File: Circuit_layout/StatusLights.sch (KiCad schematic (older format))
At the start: 6 parts

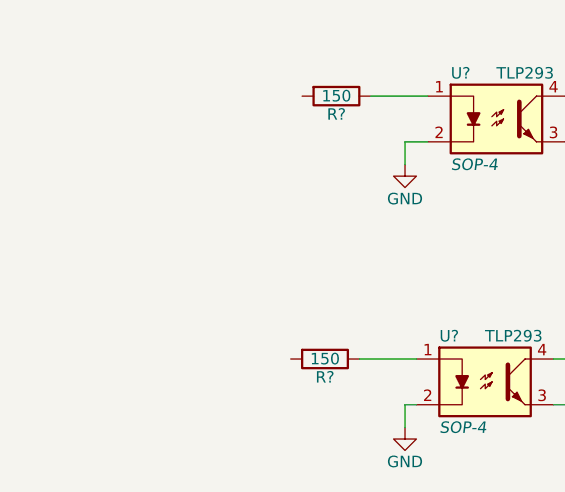
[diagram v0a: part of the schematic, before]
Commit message: adding pinouts to uController
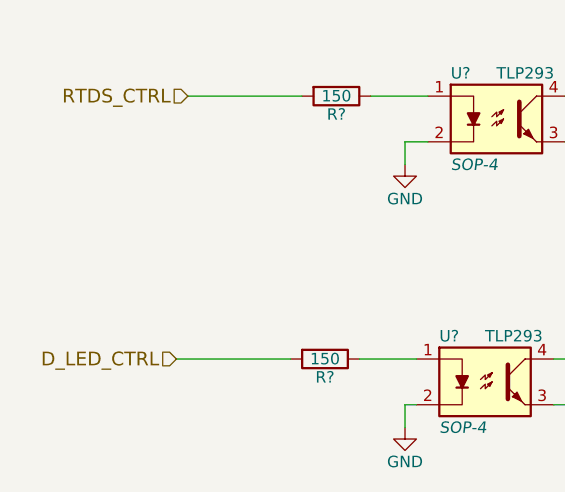
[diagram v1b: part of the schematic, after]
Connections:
- net RTDS_CTRL: now reaches R?.2
- net D_LED_CTRL: now reaches R?.2
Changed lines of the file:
@@
 Wire Wire Line
 	6450 1850 6450 1700
+Wire Wire Line
+	4600 1850 4100 1850
+Wire Wire Line
+	4550 3000 4050 3000
+Text HLabel 4050 3000 0    60   Input ~ 0
+D_LED_CTRL
+Text HLabel 4100 1850 0    60   Input ~ 0
+RTDS_CTRL
 $EndSCHEMATC

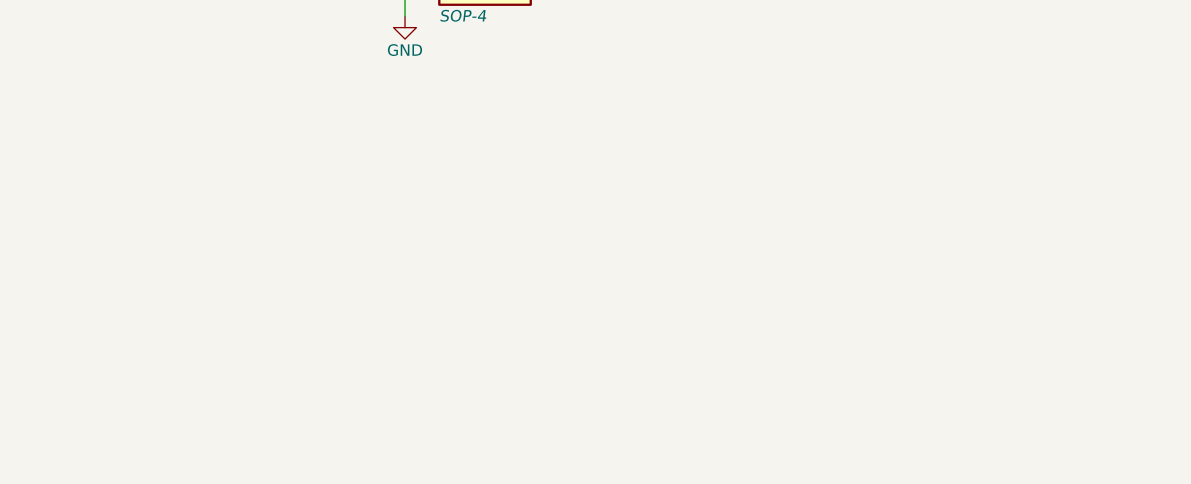
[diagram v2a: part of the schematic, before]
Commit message: added iso circuits, curr. sensor diff amp, IMD fault lt circuit, updated labels
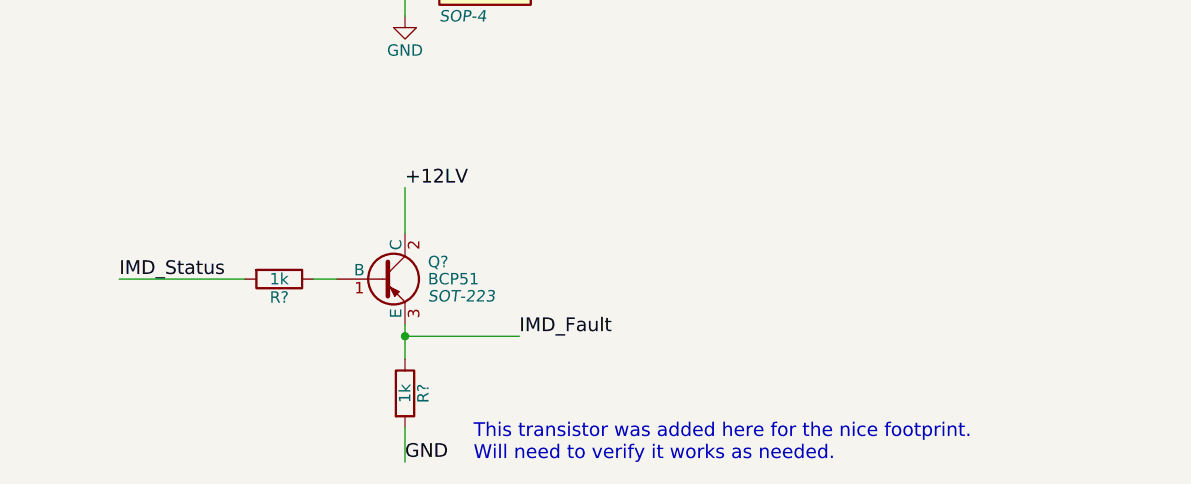
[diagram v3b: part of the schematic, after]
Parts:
- added Q?: BCP51, SOT-223, symbol BCP51
- added R? (x2): 1k, symbol R
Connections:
- net GND: now also R?.2
- new net: Q?.1 (B), R?.1
- new net +12LV: Q?.2 (C)
- new net IMD_Fault: Q?.3 (E), R?.1
- new net IMD_Status: R?.2
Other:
- note added: "This transistor was added here for the nice footprint.\nWill need to verify it works as needed."
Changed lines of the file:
@@
 EESchema Schematic File Version 2
 LIBS:Circuit_layout-rescue
+LIBS:TSI_KiCad_Lib
 LIBS:TSI_HV_Isolater-cache
 LIBS:74xgxx
@@
 $Descr A4 11693 8268
 encoding utf-8
-Sheet 5 7
+Sheet 4 7
 Title "Tractive System Interface"
 Date ""
@@
 Text HLabel 4100 1850 0    60   Input ~ 0
 RTDS_CTRL
+$Comp
+L BCP51 Q?
+U 1 1 58B1C300
+P 4950 4450
+F 0 "Q?" H 5150 4525 50  0000 L CNN
+F 1 "BCP51" H 5150 4450 50  0000 L CNN
+F 2 "SOT-223" H 5150 4375 50  0000 L CIN
+F 3 "" H 4950 4450 50  0000 L CNN
+	1    4950 4450
+	1    0    0    -1
+$EndComp
+Text Notes 5350 5250 0    60   ~ 0
+This transistor was added here for the nice footprint.\nWill need to verify it works as needed.
+Wire Wire Line
+	5050 4250 5050 4050
+$Comp
+L R R?
+U 1 1 58B1C4A9
+P 5050 4950
+F 0 "R?" V 5130 4950 50  0000 C CNN
+F 1 "1k" V 5050 4950 50  0000 C CNN
+F 2 "" V 4980 4950 50  0000 C CNN
+F 3 "" H 5050 4950 50  0000 C CNN
+	1    5050 4950
+	1    0    0    -1
+$EndComp
+$Comp
+L R R?
+U 1 1 58B1C51E
+P 4500 4450
+F 0 "R?" V 4580 4450 50  0000 C CNN
+F 1 "1k" V 4500 4450 50  0000 C CNN
+F 2 "" V 4430 4450 50  0000 C CNN
+F 3 "" H 4500 4450 50  0000 C CNN
+	1    4500 4450
+	0    1    1    0
+$EndComp
+Wire Wire Line
+	4650 4450 4750 4450
+Wire Wire Line
+	5050 4800 5050 4650
+Wire Wire Line
+	5050 4700 5550 4700
+Connection ~ 5050 4700
+Text Label 5550 4700 0    60   ~ 0
+IMD_Fault
+Text Label 3800 4450 0    60   ~ 0
+IMD_Status
+Wire Wire Line
+	3800 4450 4350 4450
+Text Label 5050 4050 0    60   ~ 0
++12LV
+Wire Wire Line
+	5050 5100 5050 5250
+Text Label 5050 5250 0    60   ~ 0
+GND
 $EndSCHEMATC

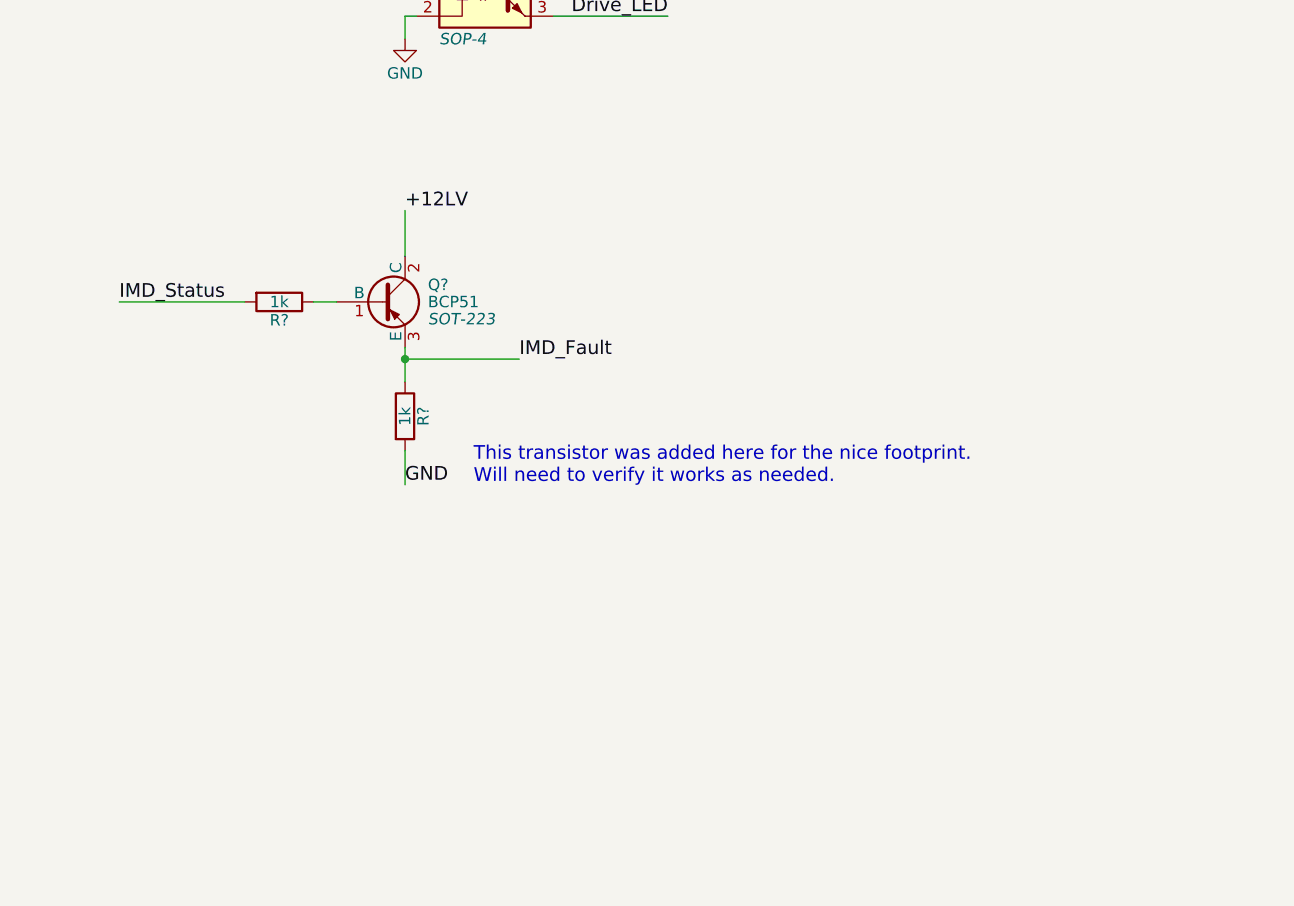
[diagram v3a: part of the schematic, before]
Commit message: added some fets
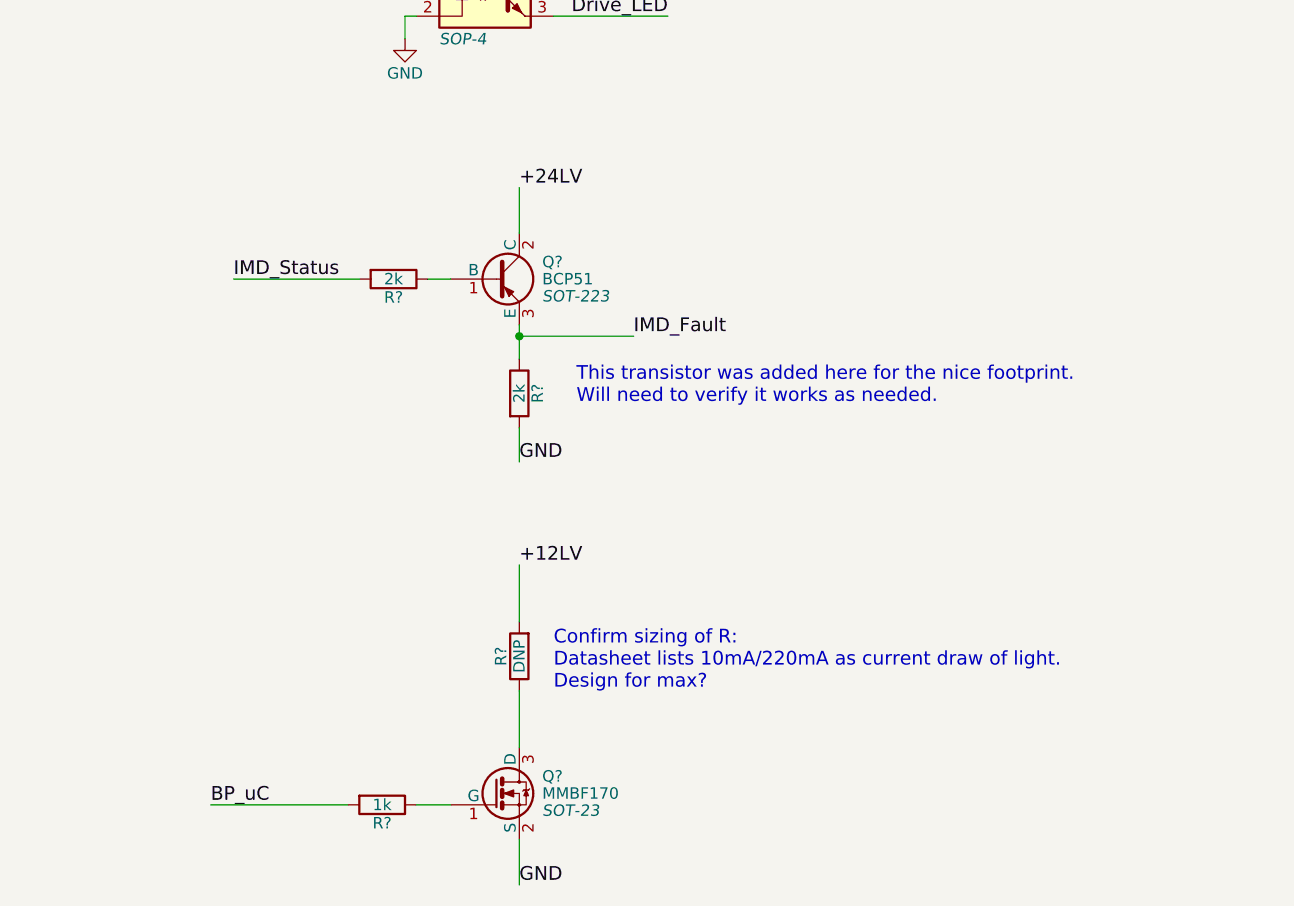
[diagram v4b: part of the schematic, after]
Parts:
- added Q?: MMBF170, SOT-23, symbol MMBF170
- added R?: 1k, symbol R
- added R?: DNP, symbol R
- R? (x2): value 1k -> 2k
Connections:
- net +12LV: now also R?.2; no longer Q?.2 (C)
- net GND: now also Q?.2 (S)
- new net: Q?.1 (G), R?.1
- new net: Q?.3 (D), R?.1
- new net +24LV: Q?.2 (C)
- new net BP_uC: R?.2
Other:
- note added: "Confirm sizing of R:\nDatasheet lists 10mA/220mA as current draw of light.\nDesign for max?"
- moved on the sheet: Q?, R?
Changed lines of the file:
@@
 LIBS:xilinx
 LIBS:Zilog
+LIBS:pacman-main-cache
 LIBS:Circuit_layout-cache
 EELAYER 25 0
@@
 L BCP51 Q?
 U 1 1 58B1C300
-P 4950 4450
-F 0 "Q?" H 5150 4525 50  0000 L CNN
-F 1 "BCP51" H 5150 4450 50  0000 L CNN
-F 2 "SOT-223" H 5150 4375 50  0000 L CIN
-F 3 "" H 4950 4450 50  0000 L CNN
-	1    4950 4450
-	1    0    0    -1
-$EndComp
-Text Notes 5350 5250 0    60   ~ 0
+P 5450 4350
+F 0 "Q?" H 5650 4425 50  0000 L CNN
+F 1 "BCP51" H 5650 4350 50  0000 L CNN
+F 2 "SOT-223" H 5650 4275 50  0000 L CIN
+F 3 "" H 5450 4350 50  0000 L CNN
+	1    5450 4350
+	1    0    0    -1
+$EndComp
+Text Notes 5800 4900 0    60   ~ 0
 This transistor was added here for the nice footprint.\nWill need to verify it works as needed.
 Wire Wire Line
-	5050 4250 5050 4050
+	5550 4150 5550 3950
 $Comp
 L R R?
 U 1 1 58B1C4A9
-P 5050 4950
-F 0 "R?" V 5130 4950 50  0000 C CNN
-F 1 "1k" V 5050 4950 50  0000 C CNN
-F 2 "" V 4980 4950 50  0000 C CNN
-F 3 "" H 5050 4950 50  0000 C CNN
-	1    5050 4950
+P 5550 4850
+F 0 "R?" V 5630 4850 50  0000 C CNN
+F 1 "2k" V 5550 4850 50  0000 C CNN
+F 2 "" V 5480 4850 50  0000 C CNN
+F 3 "" H 5550 4850 50  0000 C CNN
+	1    5550 4850
 	1    0    0    -1
 $EndComp
@@
 L R R?
 U 1 1 58B1C51E
-P 4500 4450
-F 0 "R?" V 4580 4450 50  0000 C CNN
-F 1 "1k" V 4500 4450 50  0000 C CNN
-F 2 "" V 4430 4450 50  0000 C CNN
-F 3 "" H 4500 4450 50  0000 C CNN
-	1    4500 4450
-	0    1    1    0
-$EndComp
-Wire Wire Line
-	4650 4450 4750 4450
-Wire Wire Line
-	5050 4800 5050 4650
-Wire Wire Line
-	5050 4700 5550 4700
-Connection ~ 5050 4700
-Text Label 5550 4700 0    60   ~ 0
+P 5000 4350
+F 0 "R?" V 5080 4350 50  0000 C CNN
+F 1 "2k" V 5000 4350 50  0000 C CNN
+F 2 "" V 4930 4350 50  0000 C CNN
+F 3 "" H 5000 4350 50  0000 C CNN
+	1    5000 4350
+	0    1    1    0
+$EndComp
+Wire Wire Line
+	5150 4350 5250 4350
+Wire Wire Line
+	5550 4700 5550 4550
+Wire Wire Line
+	5550 4600 6050 4600
+Connection ~ 5550 4600
+Text Label 6050 4600 0    60   ~ 0
 IMD_Fault
-Text Label 3800 4450 0    60   ~ 0
+Text Label 4300 4350 0    60   ~ 0
 IMD_Status
 Wire Wire Line
-	3800 4450 4350 4450
-Text Label 5050 4050 0    60   ~ 0
+	4300 4350 4850 4350
+Text Label 5550 3950 0    60   ~ 0
++24LV
+Wire Wire Line
+	5550 5000 5550 5150
+Text Label 5550 5150 0    60   ~ 0
+GND
+$Comp
+L R R?
+U 1 1 58B1EE45
+P 4950 6650
+F 0 "R?" V 5030 6650 50  0000 C CNN
+F 1 "1k" V 4950 6650 50  0000 C CNN
+F 2 "" V 4880 6650 50  0000 C CNN
+F 3 "" H 4950 6650 50  0000 C CNN
+	1    4950 6650
+	0    1    1    0
+$EndComp
+$Comp
+L R R?
+U 1 1 58B1EEB2
+P 5550 6000
+F 0 "R?" V 5630 6000 50  0000 C CNN
+F 1 "DNP" V 5550 6000 50  0000 C CNN
+F 2 "" V 5480 6000 50  0000 C CNN
+F 3 "" H 5550 6000 50  0000 C CNN
+	1    5550 6000
+	-1   0    0    1
+$EndComp
+Wire Wire Line
+	5550 6400 5550 6150
+Wire Wire Line
+	5250 6650 5100 6650
+Wire Wire Line
+	4800 6650 4200 6650
+Wire Wire Line
+	5550 5850 5550 5600
+Wire Wire Line
+	5550 6800 5550 7000
+Text Label 5550 5600 0    60   ~ 0
 +12LV
-Wire Wire Line
-	5050 5100 5050 5250
-Text Label 5050 5250 0    60   ~ 0
+Text Label 5550 7000 0    60   ~ 0
 GND
+Text Label 4200 6650 0    60   ~ 0
+BP_uC
+Text Notes 5700 6150 0    60   ~ 0
+Confirm sizing of R:\nDatasheet lists 10mA/220mA as current draw of light.\nDesign for max?
+$Comp
+L MMBF170 Q?
+U 1 1 58B25E37
+P 5450 6600
+F 0 "Q?" H 5650 6675 50  0000 L CNN
+F 1 "MMBF170" H 5650 6600 50  0000 L CNN
+F 2 "SOT-23" H 5650 6525 50  0000 L CIN
+F 3 "" H 5450 6600 50  0000 L CNN
+	1    5450 6600
+	1    0    0    -1
+$EndComp
 $EndSCHEMATC

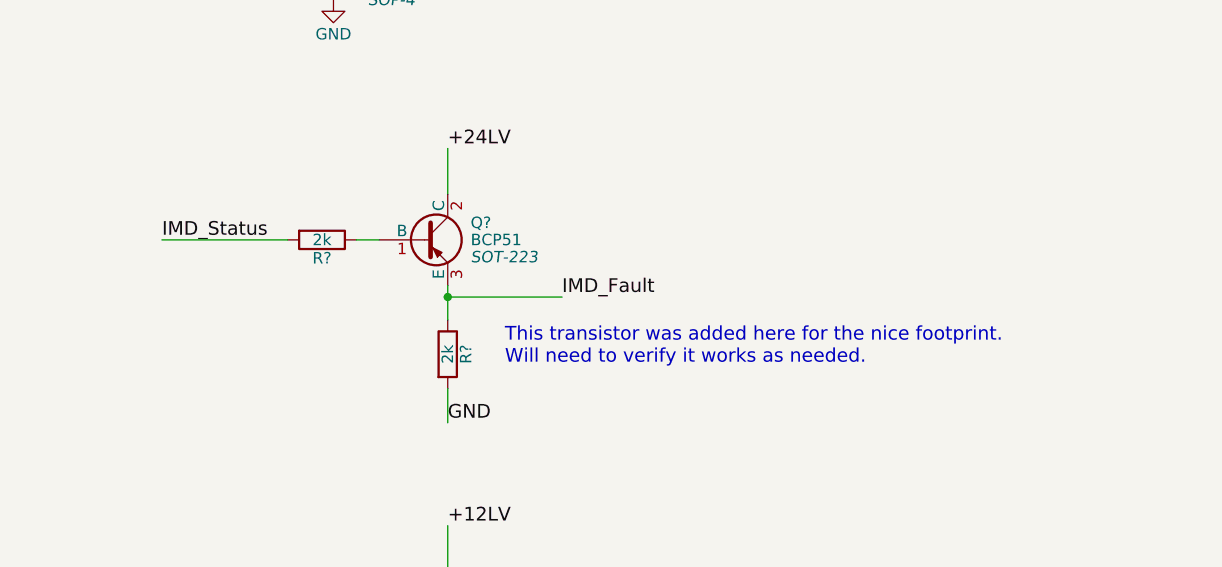
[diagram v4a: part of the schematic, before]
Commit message: changes to sch. added p-ch for use as switch
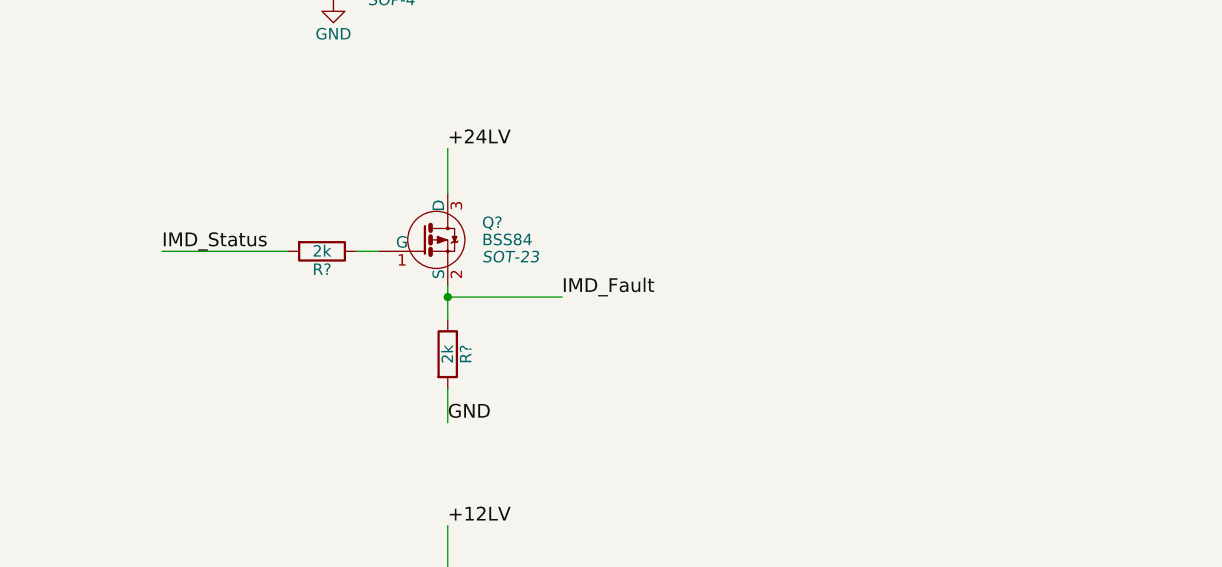
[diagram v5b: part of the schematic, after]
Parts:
- removed Q?: BCP51, SOT-223, symbol BCP51
- added Q?: BSS84, SOT-23, symbol BSS84
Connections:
- net +24LV: now also Q?.3 (D)
- net IMD_Fault: now also Q?.2 (S)
- net at R?.1: now also Q?.1 (G)
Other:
- note removed: "This transistor was added here for the nice footprint.\nWill need to verify it works as needed."
- moved on the sheet: R?
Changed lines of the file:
@@
 LIBS:Zilog
 LIBS:pacman-main-cache
+LIBS:bss84
 LIBS:Circuit_layout-cache
 EELAYER 25 0
@@
 Text HLabel 4100 1850 0    60   Input ~ 0
 RTDS_CTRL
-$Comp
-L BCP51 Q?
-U 1 1 58B1C300
-P 5450 4350
-F 0 "Q?" H 5650 4425 50  0000 L CNN
-F 1 "BCP51" H 5650 4350 50  0000 L CNN
-F 2 "SOT-223" H 5650 4275 50  0000 L CIN
-F 3 "" H 5450 4350 50  0000 L CNN
-	1    5450 4350
-	1    0    0    -1
-$EndComp
-Text Notes 5800 4900 0    60   ~ 0
-This transistor was added here for the nice footprint.\nWill need to verify it works as needed.
 Wire Wire Line
 	5550 4150 5550 3950
@@
 L R R?
 U 1 1 58B1C51E
-P 5000 4350
-F 0 "R?" V 5080 4350 50  0000 C CNN
-F 1 "2k" V 5000 4350 50  0000 C CNN
-F 2 "" V 4930 4350 50  0000 C CNN
-F 3 "" H 5000 4350 50  0000 C CNN
-	1    5000 4350
-	0    1    1    0
-$EndComp
-Wire Wire Line
-	5150 4350 5250 4350
+P 5000 4400
+F 0 "R?" V 5080 4400 50  0000 C CNN
+F 1 "2k" V 5000 4400 50  0000 C CNN
+F 2 "" V 4930 4400 50  0000 C CNN
+F 3 "" H 5000 4400 50  0000 C CNN
+	1    5000 4400
+	0    1    1    0
+$EndComp
+Wire Wire Line
+	5150 4400 5250 4400
 Wire Wire Line
 	5550 4700 5550 4550
@@
 Text Label 6050 4600 0    60   ~ 0
 IMD_Fault
-Text Label 4300 4350 0    60   ~ 0
+Text Label 4300 4400 0    60   ~ 0
 IMD_Status
 Wire Wire Line
-	4300 4350 4850 4350
+	4300 4400 4850 4400
 Text Label 5550 3950 0    60   ~ 0
 +24LV
@@
 	1    0    0    -1
 $EndComp
+$Comp
+L BSS84 Q?
+U 1 1 58B20C85
+P 5450 4350
+F 0 "Q?" H 5700 4425 50  0000 L CNN
+F 1 "BSS84" H 5700 4350 50  0000 L CNN
+F 2 "SOT-23" H 5700 4275 50  0000 L CIN
+F 3 "" H 5450 4350 50  0000 L CNN
+	1    5450 4350
+	1    0    0    -1
+$EndComp
